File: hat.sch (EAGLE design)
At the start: 17 parts, among them J1 RASPBERRYPI-40-PIN-GPIO_PTH_N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

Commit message: hat layout
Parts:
- removed +5VIN: +5V In, wirepad:2,54/1,1
- removed +5VOUT: +5V Out, wirepad:2,54/1,1
- removed GNDIN: GND In, wirepad:2,54/1,1
- removed GNDOUT: GND Out, wirepad:2,54/1,1
- removed GPIO10OUT: GPIO 10 OUT, wirepad:2,54/1,1
- removed GPIO12OUT: GPIO 12 OUT, wirepad:2,54/1,1
- removed GPIO18OUT: GPIO 18 OUT, wirepad:2,54/1,1
- removed GPIO21OUT: GPIO 21 OUT, wirepad:2,54/1,1
- added DC5VIN: DC +5V IN, SparkFun-Connectors:CONN_02PTH4
- added DC5VOUT: DC +5V OUT, SparkFun-Connectors:CONN_02PTH4
- added GPIO1012, GPIO1821: (no value), SparkFun-Connectors:CONN_02PTH4
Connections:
- removed net N$16: +5VIN.P, +5VOUT.P, C1.+, INT_5V_JMPR.2, J3.2
- new net N$18: GPIO1012.2, R2.2
- new net N$19: GPIO1821.1, R3.2
- net N$12: now also C1.+, DC5VIN.1, DC5VOUT.1, INT_5V_JMPR.2, J3.2; no longer GPIO10OUT.P, R1.2
- net N$13: now also J1.GND@9, J2.1, J3.1; no longer GPIO12OUT.P, R2.2
- net N$14: now also GPIO1012.1, R1.2; no longer GPIO18OUT.P, R3.2
- net N$15: now also GPIO1821.2; no longer GPIO21OUT.P
- net N$17: now also DC5VIN.2, DC5VOUT.2; no longer GNDIN.P, GNDOUT.P
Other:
- moved on the sheet: C1, J3, R1, R2, R3, R4

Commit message: tweaks
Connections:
- net N$1 renamed 3.3VGP10
- net N$10 renamed 5VGP18
- net N$14 renamed GP10
- net N$15 renamed GP21
- net N$18 renamed GP12
- net N$19 renamed GP18
- net N$2 renamed 3.3VGP12
- net N$3 renamed 3.3VGP18
- net N$4 renamed 3.3VGP21
- net N$5 renamed 3.3V
- net N$7 renamed 5VGP10
- net N$8 renamed 5VGP12
- net N$9 renamed 5VGP21
- removed net N$12: C1.+, DC5VIN.1, DC5VOUT.1, INT_5V_JMPR.2, J3.2
- removed net N$13: J1.GND@9, J2.1, J3.1
- removed net N$17: C1.-, DC5VIN.2, DC5VOUT.2, J1.GND@6
- removed net N$6: INT_5V_JMPR.1, J1.5V@2
- new net 5V: C1.+, DC5VIN.1, DC5VOUT.1, INT_5V_JMPR.1, INT_5V_JMPR.2, J1.5V@2, J3.2
- new net GND: C1.-, DC5VIN.2, DC5VOUT.2, J1.GND@6, J2.1, J3.1
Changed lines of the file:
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@@
 </busses>
 <nets>
-<net name="N$1" class="0">
+<net name="3.3VGP10" class="0">
 <segment>
 <pinref part="J1" gate="G$1" pin="MOSI"/>
@@
 </segment>
 </net>
-<net name="N$2" class="0">
+<net name="3.3VGP12" class="0">
 <segment>
 <pinref part="J1" gate="G$1" pin="GP12"/>
@@
 </segment>
 </net>
-<net name="N$3" class="0">
+<net name="3.3VGP18" class="0">
 <segment>
 <pinref part="J1" gate="G$1" pin="GP21"/>
@@
 </segment>
 </net>
-<net name="N$4" class="0">
+<net name="3.3VGP21" class="0">
 <segment>
 <pinref part="J1" gate="G$1" pin="GP18#"/>
@@
 </segment>
 </net>
-<net name="N$5" class="0">
+<net name="3.3V" class="0">
 <segment>
 <pinref part="J1" gate="G$1" pin="3.3V@1"/>
@@
 </segment>
 </net>
-<net name="N$6" class="0">
+<net name="5V" class="0">
 <segment>
 <pinref part="J1" gate="G$1" pin="5V@2"/>
@@
 <junction x="45.72" y="78.74"/>
 </segment>
-</net>
-<net name="N$7" class="0">
-<segment>
-<pinref part="J3" gate="G$1" pin="6"/>
-<junction x="109.22" y="66.04"/>
-<wire x1="109.22" y1="66.04" x2="124.46" y2="66.04" width="0.1524" layer="91"/>
-<wire x1="124.46" y1="66.04" x2="124.46" y2="76.2" width="0.1524" layer="91"/>
-<pinref part="R1" gate="G$1" pin="1"/>
-<wire x1="124.46" y1="76.2" x2="137.16" y2="76.2" width="0.1524" layer="91"/>
-<junction x="137.16" y="76.2"/>
-</segment>
-</net>
-<net name="N$8" class="0">
-<segment>
-<pinref part="J3" gate="G$1" pin="5"/>
-<junction x="109.22" y="63.5"/>
-<wire x1="109.22" y1="63.5" x2="134.62" y2="63.5" width="0.1524" layer="91"/>
-<wire x1="134.62" y1="63.5" x2="134.62" y2="66.04" width="0.1524" layer="91"/>
-<pinref part="R2" gate="G$1" pin="1"/>
-<wire x1="134.62" y1="66.04" x2="137.16" y2="66.04" width="0.1524" layer="91"/>
-<junction x="137.16" y="66.04"/>
-</segment>
-</net>
-<net name="N$9" class="0">
-<segment>
-<pinref part="J3" gate="G$1" pin="3"/>
-<junction x="109.22" y="58.42"/>
-<wire x1="109.22" y1="58.42" x2="124.46" y2="58.42" width="0.1524" layer="91"/>
-<wire x1="124.46" y1="58.42" x2="124.46" y2="45.72" width="0.1524" layer="91"/>
-<pinref part="R4" gate="G$1" pin="1"/>
-<wire x1="124.46" y1="45.72" x2="137.16" y2="45.72" width="0.1524" layer="91"/>
-<junction x="137.16" y="45.72"/>
-</segment>
-</net>
-<net name="N$10" class="0">
-<segment>
-<pinref part="J3" gate="G$1" pin="4"/>
-<junction x="109.22" y="60.96"/>
-<wire x1="109.22" y1="60.96" x2="134.62" y2="60.96" width="0.1524" layer="91"/>
-<wire x1="134.62" y1="60.96" x2="134.62" y2="55.88" width="0.1524" layer="91"/>
-<pinref part="R3" gate="G$1" pin="1"/>
-<wire x1="134.62" y1="55.88" x2="137.16" y2="55.88" width="0.1524" layer="91"/>
-<junction x="137.16" y="55.88"/>
-</segment>
-</net>
-<net name="N$15" class="0">
-<segment>
-<pinref part="R4" gate="G$1" pin="2"/>
-<wire x1="149.86" y1="45.72" x2="147.32" y2="45.72" width="0.1524" layer="91"/>
-<pinref part="GPIO1821" gate="G$1" pin="2"/>
-<wire x1="147.32" y1="45.72" x2="157.48" y2="45.72" width="0.1524" layer="91"/>
-<wire x1="157.48" y1="45.72" x2="157.48" y2="50.8" width="0.1524" layer="91"/>
-<junction x="147.32" y="45.72"/>
-</segment>
-</net>
-<net name="N$17" class="0">
-<segment>
-<wire x1="58.42" y1="91.44" x2="-12.7" y2="91.44" width="0.1524" layer="91"/>
-<wire x1="-12.7" y1="91.44" x2="-12.7" y2="40.64" width="0.1524" layer="91"/>
-<pinref part="J1" gate="G$1" pin="GND@6"/>
-<wire x1="-12.7" y1="40.64" x2="-5.08" y2="40.64" width="0.1524" layer="91"/>
-<junction x="-5.08" y="40.64"/>
-<wire x1="58.42" y1="91.44" x2="58.42" y2="116.84" width="0.1524" layer="91"/>
-<pinref part="DC5VIN" gate="G$1" pin="2"/>
-<wire x1="66.04" y1="104.14" x2="66.04" y2="101.6" width="0.1524" layer="91"/>
-<pinref part="DC5VOUT" gate="G$1" pin="2"/>
-<wire x1="66.04" y1="101.6" x2="76.2" y2="101.6" width="0.1524" layer="91"/>
-<wire x1="76.2" y1="101.6" x2="86.36" y2="101.6" width="0.1524" layer="91"/>
-<wire x1="86.36" y1="101.6" x2="86.36" y2="104.14" width="0.1524" layer="91"/>
-<pinref part="C1" gate="G$1" pin="-"/>
-<junction x="76.2" y="101.6"/>
-<wire x1="58.42" y1="116.84" x2="76.2" y2="116.84" width="0.1524" layer="91"/>
-<wire x1="76.2" y1="116.84" x2="76.2" y2="101.6" width="0.1524" layer="91"/>
-</segment>
-</net>
-<net name="N$12" class="0">
 <segment>
 <pinref part="DC5VIN" gate="G$1" pin="1"/>
@@
 <junction x="109.22" y="55.88"/>
 <pinref part="INT_5V_JMPR" gate="G$1" pin="2"/>
-<wire x1="55.88" y1="78.74" x2="76.2" y2="78.74" width="0.1524" layer="91"/>
+<wire x1="55.88" y1="78.74" x2="76.2" y2="78.74" width="0.0762" layer="91"/>
 <wire x1="76.2" y1="78.74" x2="119.38" y2="78.74" width="0.1524" layer="91"/>
 <wire x1="119.38" y1="78.74" x2="119.38" y2="55.88" width="0.1524" layer="91"/>
@@
 </segment>
 </net>
-<net name="N$13" class="0">
+<net name="5VGP10" class="0">
 <segment>
-<pinref part="J1" gate="G$1" pin="GND@9"/>
-<wire x1="-5.08" y1="38.1" x2="-12.7" y2="38.1" width="0.1524" layer="91"/>
-<wire x1="-12.7" y1="38.1" x2="-12.7" y2="12.7" width="0.1524" layer="91"/>
-<pinref part="J2" gate="G$1" pin="1"/>
-<wire x1="-12.7" y1="12.7" x2="68.58" y2="12.7" width="0.1524" layer="91"/>
-<wire x1="68.58" y1="12.7" x2="68.58" y2="53.34" width="0.1524" layer="91"/>
-<pinref part="J3" gate="G$1" pin="1"/>
-<wire x1="68.58" y1="53.34" x2="109.22" y2="53.34" width="0.1524" layer="91"/>
-<junction x="68.58" y="53.34"/>
+<pinref part="J3" gate="G$1" pin="6"/>
+<junction x="109.22" y="66.04"/>
+<wire x1="109.22" y1="66.04" x2="124.46" y2="66.04" width="0.1524" layer="91"/>
+<wire x1="124.46" y1="66.04" x2="124.46" y2="76.2" width="0.1524" layer="91"/>
+<pinref part="R1" gate="G$1" pin="1"/>
+<wire x1="124.46" y1="76.2" x2="137.16" y2="76.2" width="0.1524" layer="91"/>
+<junction x="137.16" y="76.2"/>
 </segment>
 </net>
-<net name="N$14" class="0">
+<net name="5VGP12" class="0">
+<segment>
+<pinref part="J3" gate="G$1" pin="5"/>
+<junction x="109.22" y="63.5"/>
+<wire x1="109.22" y1="63.5" x2="134.62" y2="63.5" width="0.1524" layer="91"/>
+<wire x1="134.62" y1="63.5" x2="134.62" y2="66.04" width="0.1524" layer="91"/>
+<pinref part="R2" gate="G$1" pin="1"/>
+<wire x1="134.62" y1="66.04" x2="137.16" y2="66.04" width="0.1524" layer="91"/>
+<junction x="137.16" y="66.04"/>
+</segment>
+</net>
+<net name="5VGP21" class="0">
+<segment>
+<pinref part="J3" gate="G$1" pin="3"/>
+<junction x="109.22" y="58.42"/>
+<wire x1="109.22" y1="58.42" x2="124.46" y2="58.42" width="0.1524" layer="91"/>
+<wire x1="124.46" y1="58.42" x2="124.46" y2="45.72" width="0.1524" layer="91"/>
+<pinref part="R4" gate="G$1" pin="1"/>
+<wire x1="124.46" y1="45.72" x2="137.16" y2="45.72" width="0.1524" layer="91"/>
+<junction x="137.16" y="45.72"/>
+</segment>
+</net>
+<net name="5VGP18" class="0">
+<segment>
+<pinref part="J3" gate="G$1" pin="4"/>
+<junction x="109.22" y="60.96"/>
+<wire x1="109.22" y1="60.96" x2="134.62" y2="60.96" width="0.1524" layer="91"/>
+<wire x1="134.62" y1="60.96" x2="134.62" y2="55.88" width="0.1524" layer="91"/>
+<pinref part="R3" gate="G$1" pin="1"/>
+<wire x1="134.62" y1="55.88" x2="137.16" y2="55.88" width="0.1524" layer="91"/>
+<junction x="137.16" y="55.88"/>
+</segment>
+</net>
+<net name="GP21" class="0">
+<segment>
+<pinref part="R4" gate="G$1" pin="2"/>
+<wire x1="149.86" y1="45.72" x2="147.32" y2="45.72" width="0.1524" layer="91"/>
+<pinref part="GPIO1821" gate="G$1" pin="2"/>
+<wire x1="147.32" y1="45.72" x2="157.48" y2="45.72" width="0.1524" layer="91"/>
+<wire x1="157.48" y1="45.72" x2="157.48" y2="50.8" width="0.1524" layer="91"/>
+<junction x="147.32" y="45.72"/>
+</segment>
+</net>
+<net name="GND" class="0">
+<segment>
+<wire x1="58.42" y1="91.44" x2="-12.7" y2="91.44" width="0.1524" layer="91"/>
+<wire x1="-12.7" y1="91.44" x2="-12.7" y2="40.64" width="0.1524" layer="91"/>
+<pinref part="J1" gate="G$1" pin="GND@6"/>
+<wire x1="-12.7" y1="40.64" x2="-5.08" y2="40.64" width="0.1524" layer="91"/>
+<junction x="-5.08" y="40.64"/>
+<wire x1="58.42" y1="91.44" x2="58.42" y2="116.84" width="0.1524" layer="91"/>
+<pinref part="DC5VIN" gate="G$1" pin="2"/>
+<wire x1="66.04" y1="104.14" x2="66.04" y2="101.6" width="0.1524" layer="91"/>
+<pinref part="DC5VOUT" gate="G$1" pin="2"/>
+<wire x1="66.04" y1="101.6" x2="76.2" y2="101.6" width="0.1524" layer="91"/>
+<wire x1="86.36" y1="101.6" x2="86.36" y2="104.14" width="0.1524" layer="91"/>
+<pinref part="C1" gate="G$1" pin="-"/>
+<junction x="76.2" y="101.6"/>
+<wire x1="58.42" y1="116.84" x2="76.2" y2="116.84" width="0.1524" layer="91"/>
+<wire x1="76.2" y1="116.84" x2="76.2" y2="101.6" width="0.1524" layer="91"/>
+<wire x1="76.2" y1="101.6" x2="86.36" y2="101.6" width="0.1524" layer="91"/>
+<pinref part="J3" gate="G$1" pin="1"/>
+<pinref part="J2" gate="G$1" pin="1"/>
+<wire x1="68.58" y1="53.34" x2="86.36" y2="53.34" width="0.1524" layer="91"/>
+<wire x1="86.36" y1="53.34" x2="109.22" y2="53.34" width="0.1524" layer="91"/>
+<wire x1="86.36" y1="101.6" x2="86.36" y2="53.34" width="0.1524" layer="91"/>
+<junction x="86.36" y="101.6"/>
+<junction x="86.36" y="53.34"/>
+</segment>
+</net>
+<net name="GP10" class="0">
 <segment>
 <pinref part="R1" gate="G$1" pin="2"/>
@@
 </segment>
 </net>
-<net name="N$18" class="0">
+<net name="GP12" class="0">
 <segment>
 <pinref part="R2" gate="G$1" pin="2"/>
@@
 </segment>
 </net>
-<net name="N$19" class="0">
+<net name="GP18" class="0">
 <segment>
 <pinref part="R3" gate="G$1" pin="2"/>

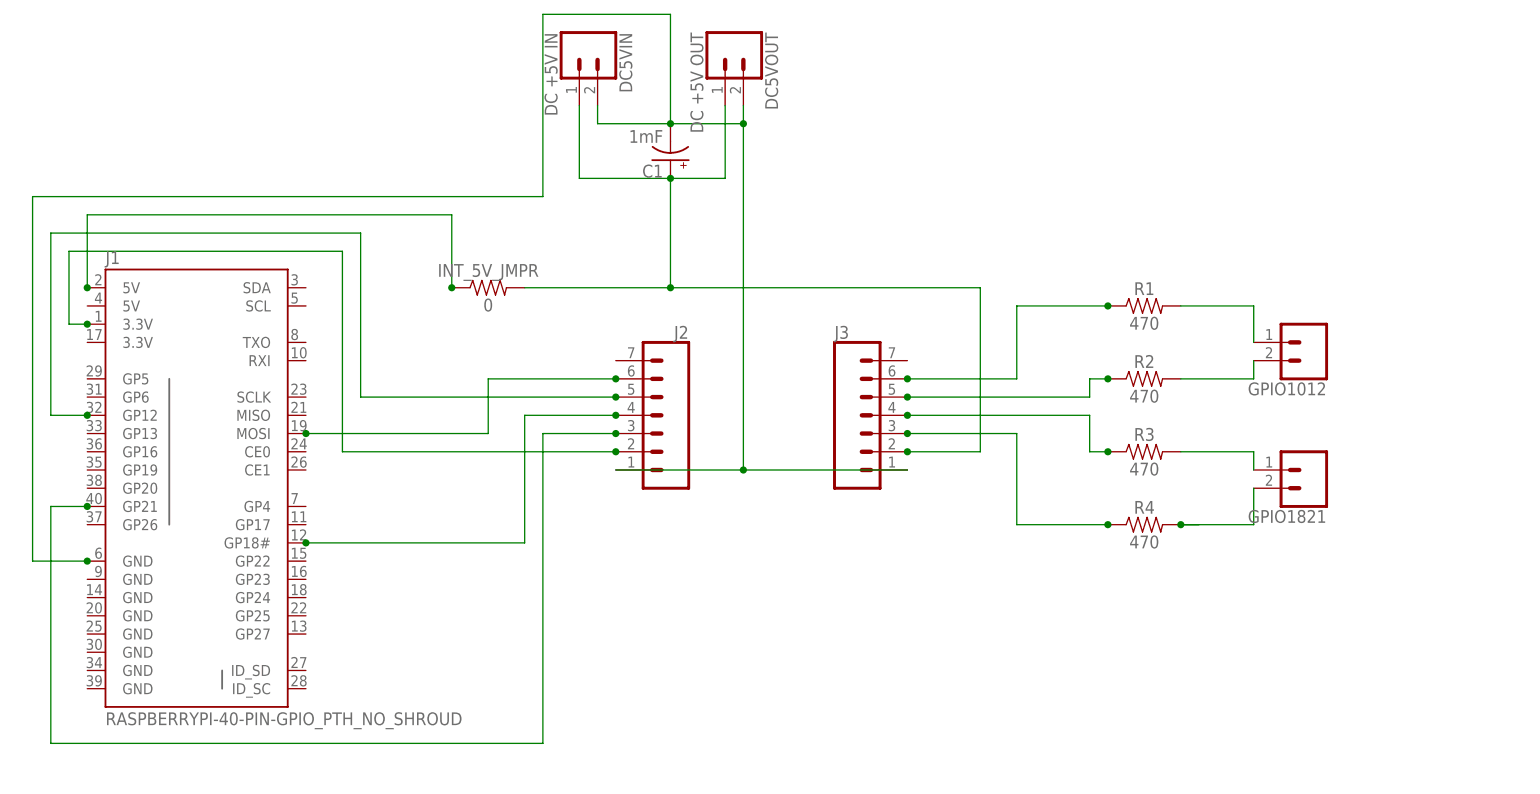
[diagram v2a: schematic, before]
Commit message: shrunk board, double sided
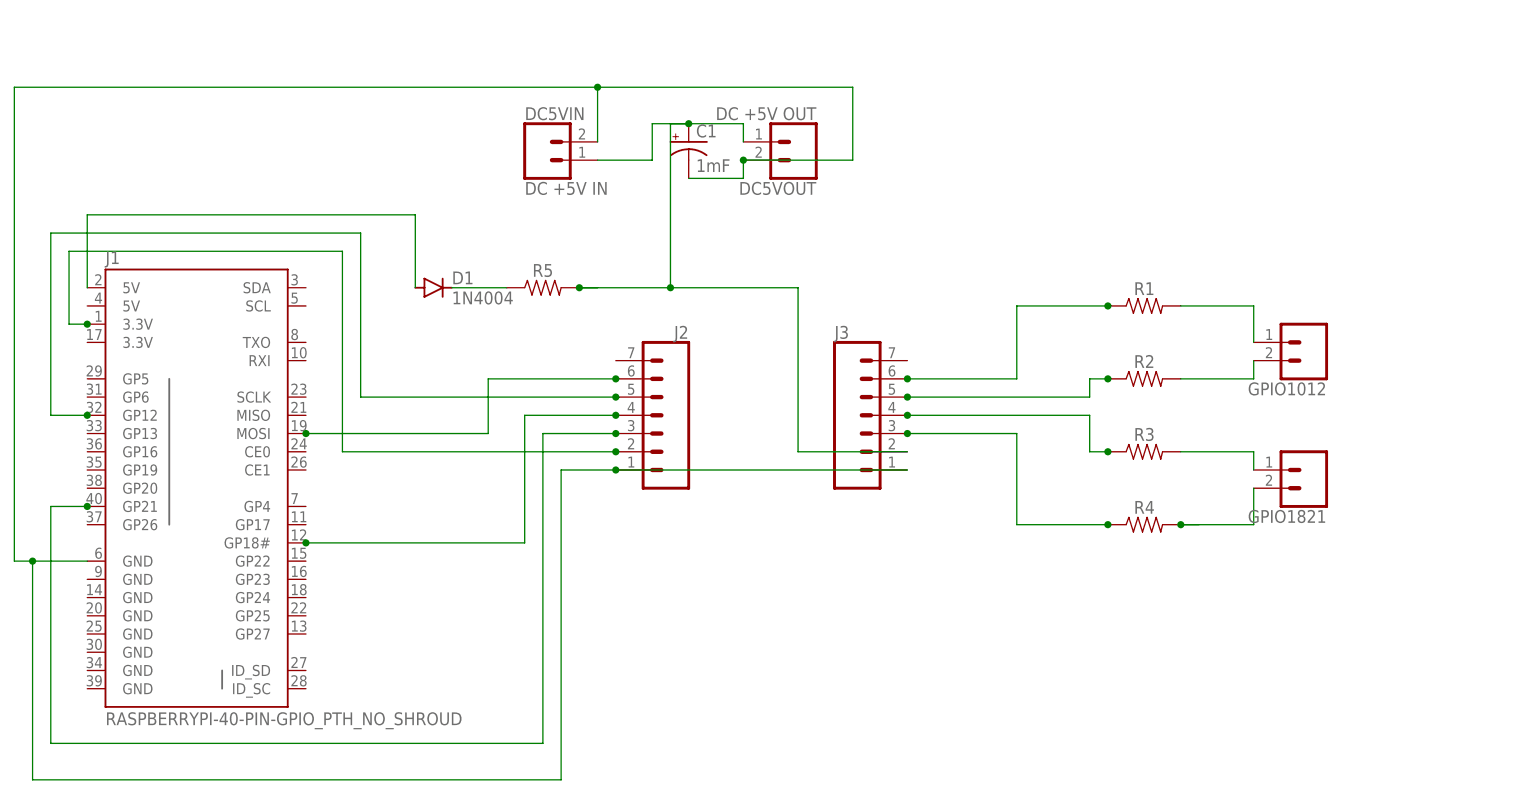
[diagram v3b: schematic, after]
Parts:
- removed INT_5V_JMPR: 0, SparkFun-Resistors:0OHM-0603-1/10W-5%
- added D1: 1N4004, diode:1N4004
- added R5: (no value), SparkFun-Resistors:RESISTORAXIAL-0.3
- R1, R2, R3, R4: value 470 -> (none); device SparkFun-Resistors:470OHM-0603-1/10W-1% -> SparkFun-Resistors:RESISTORAXIAL-0.3
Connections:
- new net N$5: D1.C, R5.1
- new net N$6: C1.+, DC5VIN.1, DC5VOUT.1, J3.2, R5.2
- net 3.3VGP18: now also J1.GP18#, J2.4; no longer J1.GP21, J2.3
- net 3.3VGP21: now also J1.GP21, J2.3; no longer J1.GP18#, J2.4
- net 5V: now also D1.A; no longer C1.+, DC5VIN.1, DC5VOUT.1, INT_5V_JMPR.1, INT_5V_JMPR.2, J3.2
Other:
- moved on the sheet: C1, DC5VIN, DC5VOUT
